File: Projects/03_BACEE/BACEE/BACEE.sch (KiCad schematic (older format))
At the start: 13 parts, among them U1 DS1337_MLv1, U2 24LC1025, U3 24LC1025, U4 ATmega328P-AU, Y1 Crystal, Y2 Crystal

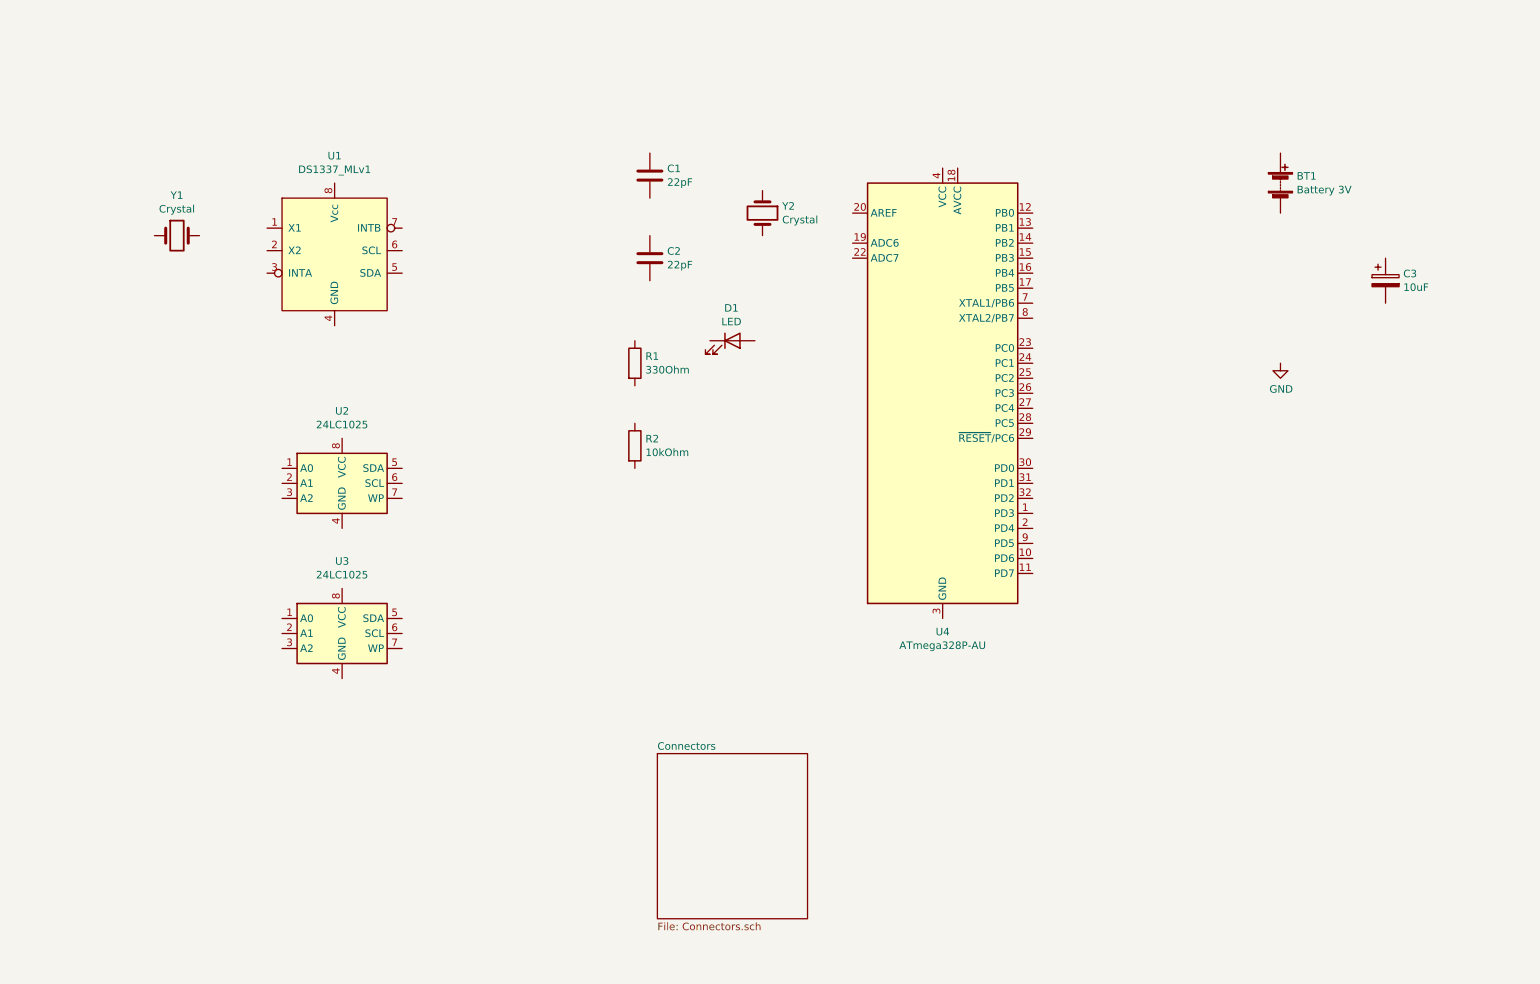
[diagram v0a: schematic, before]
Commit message: Project 3: Complete wiring of connectors hierarchical sheet
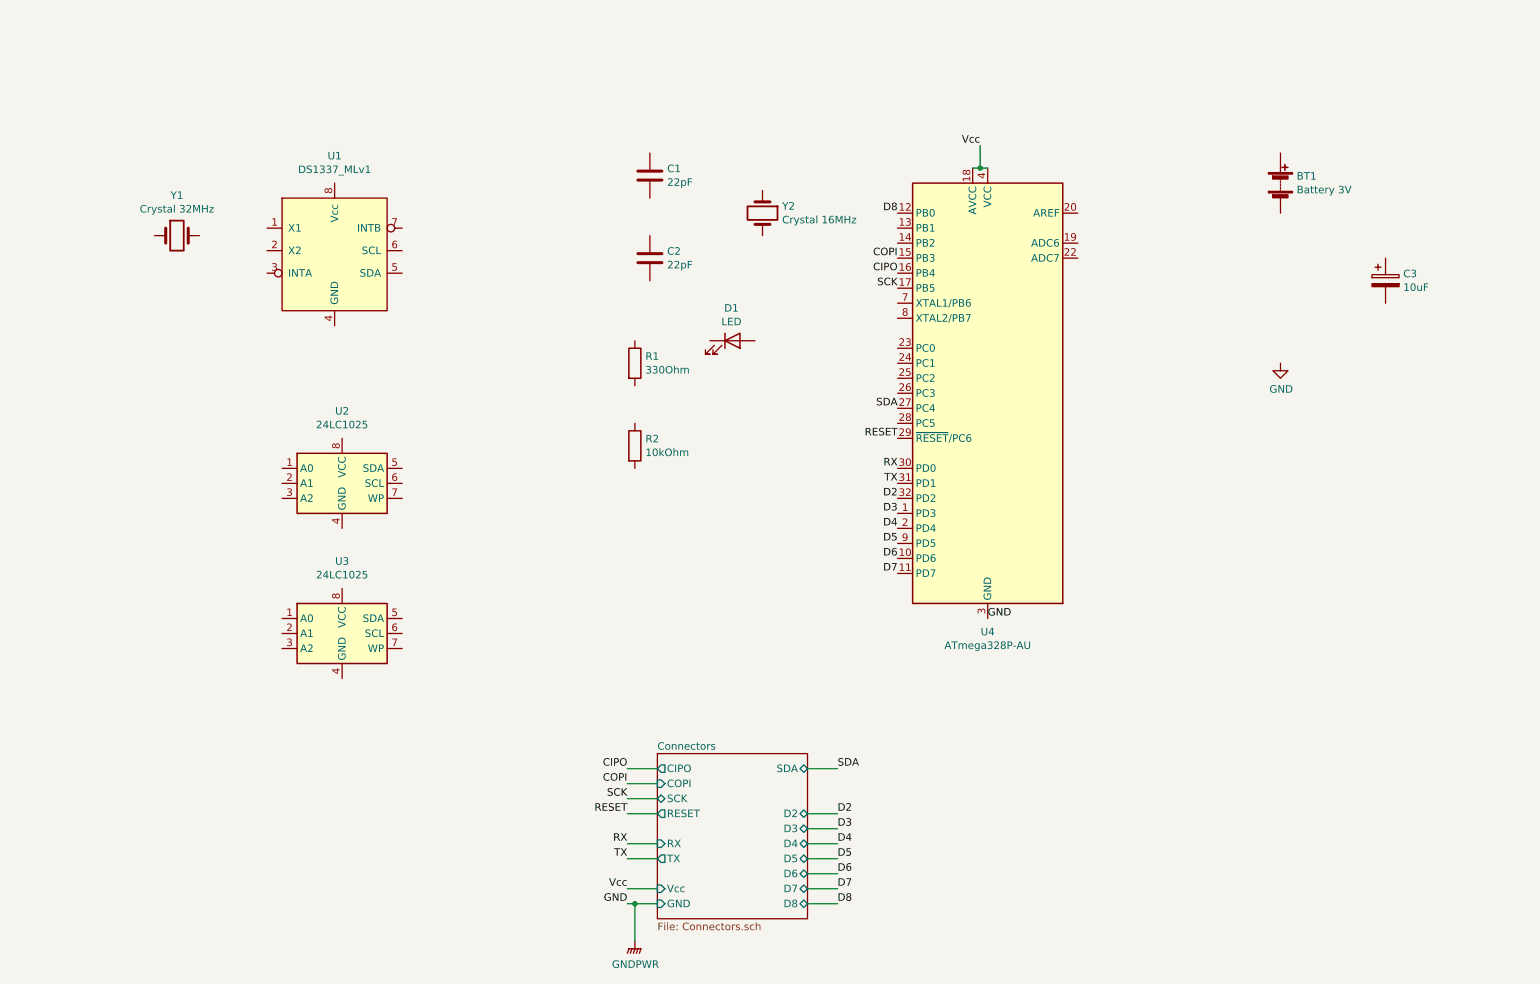
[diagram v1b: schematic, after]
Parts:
- Y1: value Crystal -> Crystal 32MHz
- Y2: value Crystal -> Crystal 16MHz
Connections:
- net GND: now also U4.21 (GND), U4.3 (GND), U4.5 (GND)
- net D3: now reaches U4.1 (PD3)
- net D6: now reaches U4.10 (PD6)
- net D7: now reaches U4.11 (PD7)
- net D8: now reaches U4.12 (PB0)
- net COPI: now reaches U4.15 (PB3)
- net CIPO: now reaches U4.16 (PB4)
- net SCK: now reaches U4.17 (PB5)
- net Vcc: now reaches U4.18 (AVCC)
- net Vcc: now also U4.4 (VCC), U4.6 (VCC)
- net D4: now reaches U4.2 (PD4)
- net SDA: now reaches U4.27 (PC4)
- net RESET: now reaches U4.29 (~RESET~/PC6)
- net RX: now reaches U4.30 (PD0)
- net TX: now reaches U4.31 (PD1)
- net D2: now reaches U4.32 (PD2)
- net D5: now reaches U4.9 (PD5)
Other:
- moved on the sheet: U4
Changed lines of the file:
@@
-	1    0    0    -1
-$EndComp
-$Sheet
-S 5100 5900 1000 1100
-U 61D27AD2
-F0 "Connectors" 50
-F1 "Connectors.sch" 50
-$EndSheet
-$Comp
-L MCU_Microchip_ATmega:ATmega328P-AU U4
-U 1 1 61D2E20A
-P 7000 3500
-F 0 "U4" H 7000 1911 50  0000 C CNN
-F 1 "ATmega328P-AU" H 7000 1820 50  0000 C CNN
-F 2 "Package_QFP:TQFP-32_7x7mm_P0.8mm" H 7000 3500 50  0001 C CIN
-F 3 "http://ww1.microchip.com/downloads/en/DeviceDoc/ATmega328_P%20AVR%20MCU%20with%20picoPower%20Technology%20Data%20Sheet%2040001984A.pdf" H 7000 3500 50  0001 C CNN
-	1    7000 3500
 	1    0    0    -1
 $EndComp
@@
 P 5800 2300
 F 0 "Y2" V 5754 2431 50  0000 L CNN
-F 1 "Crystal" V 5845 2431 50  0000 L CNN
+F 1 "Crystal 16MHz" V 5845 2431 50  0000 L CNN
 F 2 "Crystal:Crystal_SMD_5032-2Pin_5.0x3.2mm_HandSoldering" H 5800 2300 50  0001 C CNN
 F 3 "~" H 5800 2300 50  0001 C CNN
@@
 P 1900 2450
 F 0 "Y1" H 1900 2718 50  0000 C CNN
-F 1 "Crystal" H 1900 2627 50  0000 C CNN
+F 1 "Crystal 32MHz" H 1900 2627 50  0000 C CNN
 F 2 "Crystal:Crystal_SMD_MicroCrystal_CC7V-T1A-2Pin_3.2x1.5mm" H 1900 2450 50  0001 C CNN
 F 3 "~" H 1900 2450 50  0001 C CNN
@@
 	1    0    0    -1
 $EndComp
+Text Label 4900 6000 2    50   ~ 0
+CIPO
+Text Label 6700 2700 2    50   ~ 0
+CIPO
+$Comp
+L MCU_Microchip_ATmega:ATmega328P-AU U4
+U 1 1 61D2E20A
+P 7300 3500
+F 0 "U4" H 7300 1911 50  0000 C CNN
+F 1 "ATmega328P-AU" H 7300 1820 50  0000 C CNN
+F 2 "Package_QFP:TQFP-32_7x7mm_P0.8mm" H 7300 3500 50  0001 C CIN
+F 3 "http://ww1.microchip.com/downloads/en/DeviceDoc/ATmega328_P%20AVR%20MCU%20with%20picoPower%20Technology%20Data%20Sheet%2040001984A.pdf" H 7300 3500 50  0001 C CNN
+	1    7300 3500
+	-1   0    0    -1
+$EndComp
+Wire Wire Line
+	5100 6000 4900 6000
+Text Label 4900 6200 2    50   ~ 0
+SCK
+Wire Wire Line
+	5100 6200 4900 6200
+Text Label 4900 6300 2    50   ~ 0
+RESET
+Wire Wire Line
+	5100 6300 4900 6300
+Text Label 4900 6800 2    50   ~ 0
+Vcc
+Wire Wire Line
+	5100 6800 4900 6800
+Text Label 4900 6100 2    50   ~ 0
+COPI
+Wire Wire Line
+	5100 6100 4900 6100
+Text Label 4900 6900 2    50   ~ 0
+GND
+Wire Wire Line
+	5100 6900 4950 6900
+Text Label 6700 3800 2    50   ~ 0
+RESET
+Text Label 6700 2600 2    50   ~ 0
+COPI
+Text Label 6700 2800 2    50   ~ 0
+SCK
+Text Label 7250 1850 2    50   ~ 0
+Vcc
+Wire Wire Line
+	7200 2000 7250 2000
+Wire Wire Line
+	7250 1850 7250 2000
+Connection ~ 7250 2000
+Wire Wire Line
+	7250 2000 7300 2000
+Text Label 7300 5000 0    50   ~ 0
+GND
+$Comp
+L power:GNDPWR #PWR?
+U 1 1 61D4A407
+P 4950 7150
+F 0 "#PWR?" H 4950 6950 50  0001 C CNN
+F 1 "GNDPWR" H 4954 6996 50  0000 C CNN
+F 2 "" H 4950 7100 50  0001 C CNN
+F 3 "" H 4950 7100 50  0001 C CNN
+	1    4950 7150
+	1    0    0    -1
+$EndComp
+Wire Wire Line
+	4950 7150 4950 6900
+Connection ~ 4950 6900
+Wire Wire Line
+	4950 6900 4900 6900
+Wire Wire Line
+	6300 6000 6100 6000
+Text Label 6300 6000 0    50   ~ 0
+SDA
+Text Label 6700 4300 2    50   ~ 0
+D3
+Text Label 6700 4200 2    50   ~ 0
+D2
+Text Label 6700 4400 2    50   ~ 0
+D4
+Text Label 6700 4500 2    50   ~ 0
+D5
+Text Label 6700 4600 2    50   ~ 0
+D6
+Text Label 6700 4700 2    50   ~ 0
+D7
+Text Label 6700 2300 2    50   ~ 0
+D8
+Text Label 6700 3600 2    50   ~ 0
+SDA
+Wire Wire Line
+	5100 6500 4900 6500
+Wire Wire Line
+	5100 6600 4900 6600
+Text Label 4900 6500 2    50   ~ 0
+RX
+Text Label 4900 6600 2    50   ~ 0
+TX
+Text Label 6700 4000 2    50   ~ 0
+RX
+Text Label 6700 4100 2    50   ~ 0
+TX
+Text Label 6300 6900 0    50   ~ 0
+D8
+Text Label 6300 6800 0    50   ~ 0
+D7
+Text Label 6300 6700 0    50   ~ 0
+D6
+Text Label 6300 6600 0    50   ~ 0
+D5
+Text Label 6300 6500 0    50   ~ 0
+D4
+Text Label 6300 6400 0    50   ~ 0
+D3
+Text Label 6300 6300 0    50   ~ 0
+D2
+Wire Wire Line
+	6300 6900 6100 6900
+Wire Wire Line
+	6300 6800 6100 6800
+Wire Wire Line
+	6300 6700 6100 6700
+Wire Wire Line
+	6300 6600 6100 6600
+Wire Wire Line
+	6300 6500 6100 6500
+Wire Wire Line
+	6300 6400 6100 6400
+Wire Wire Line
+	6300 6300 6100 6300
+$Sheet
+S 5100 5900 1000 1100
+U 61D27AD2
+F0 "Connectors" 50
+F1 "Connectors.sch" 50
+F2 "CIPO" O L 5100 6000 50
+F3 "SCK" B L 5100 6200 50
+F4 "RESET" O L 5100 6300 50
+F5 "Vcc" I L 5100 6800 50
+F6 "COPI" I L 5100 6100 50
+F7 "GND" I L 5100 6900 50
+F8 "RX" I L 5100 6500 50
+F9 "TX" O L 5100 6600 50
+F10 "SDA" B R 6100 6000 50
+F11 "D2" B R 6100 6300 50
+F12 "D3" B R 6100 6400 50
+F13 "D4" B R 6100 6500 50
+F14 "D5" B R 6100 6600 50
+F15 "D6" B R 6100 6700 50
+F16 "D7" B R 6100 6800 50
+F17 "D8" B R 6100 6900 50
+$EndSheet
 $EndSCHEMATC

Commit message: Project 3: Finish wiring and naming nets in root sheet
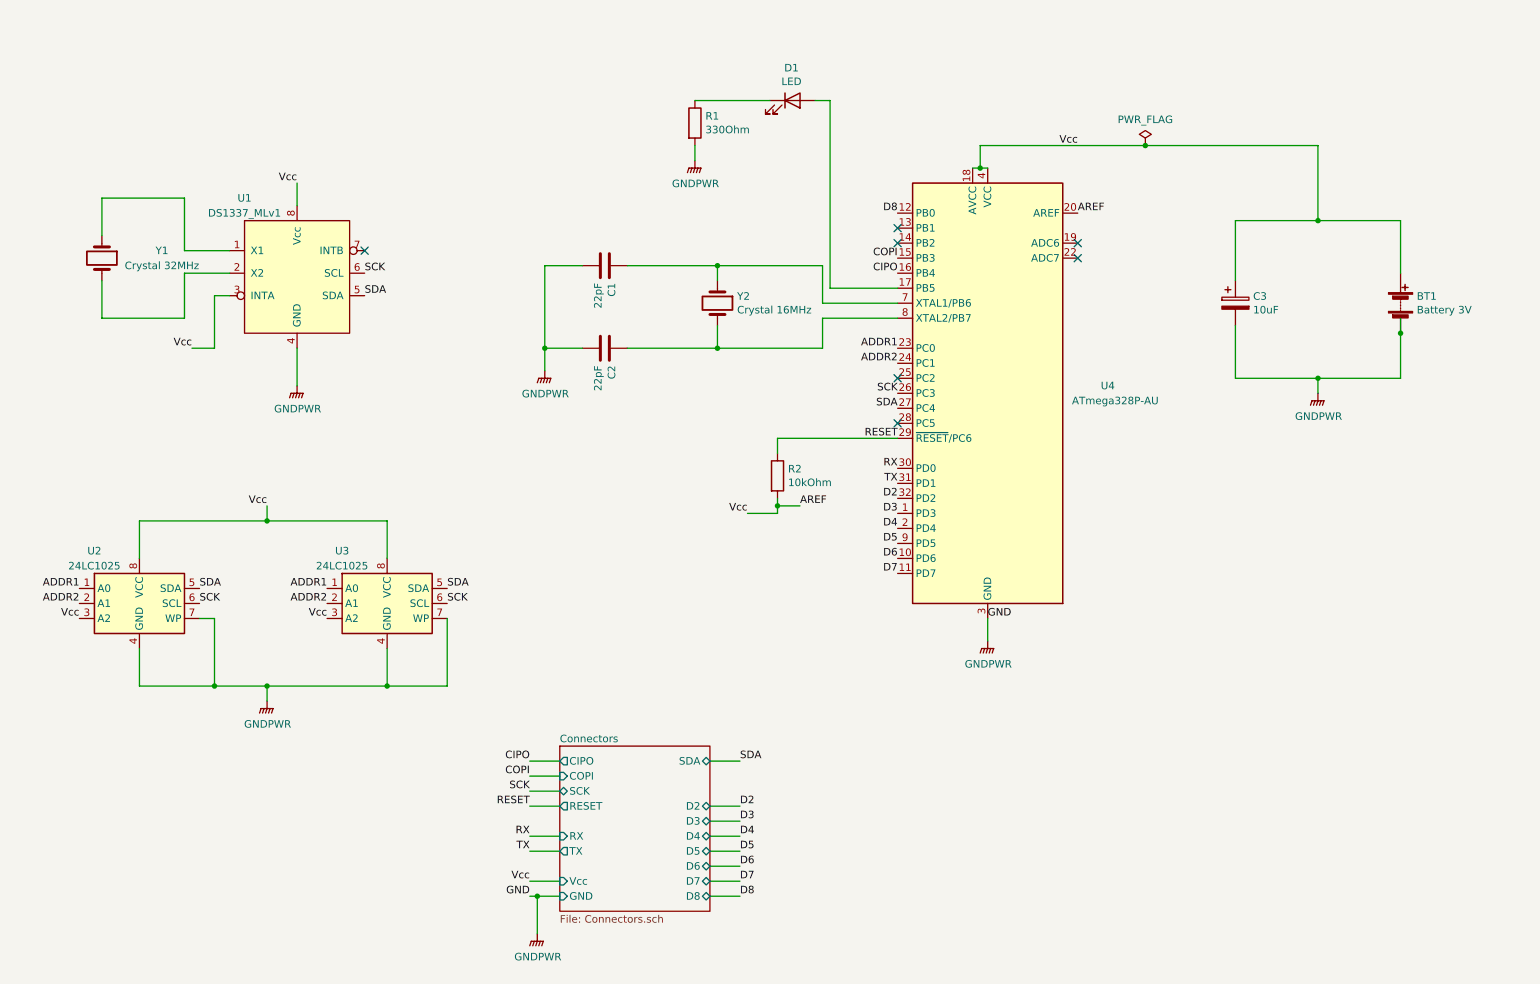
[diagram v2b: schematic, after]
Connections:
- net GND is gone; now on net GNDPWR: U4.21 (GND), U4.3 (GND), U4.5 (GND)
- net Vcc is gone; now on net AREF: U4.18 (AVCC), U4.4 (VCC), U4.6 (VCC)
- net RESET: now also R2.1
- net SCK: now also U1.6 (SCL), U2.6 (SCL), U3.6 (SCL), U4.26 (PC3); no longer U4.17 (PB5)
- net SDA: now also U1.5 (SDA), U2.5 (SDA), U3.5 (SDA)
- net AREF: now reaches BT1.1 (+)
- net AREF: now also C3.1, R2.2, U1.3 (INTA), U1.8 (Vcc), U2.3 (A2), U2.8 (VCC), U3.3 (A2), U3.8 (VCC), U4.20 (AREF)
- net GNDPWR: now reaches BT1.2 (-)
- net GNDPWR: now also C1.2, C2.2, C3.2, R1.2, U1.4 (GND), U2.4 (GND), U2.7 (WP), U3.4 (GND), U3.7 (WP)
- net at D1.1 (K): now also R1.1
- net at D1.2 (A): now also U4.17 (PB5)
- net at C1.1: now also U4.7 (XTAL1/PB6), Y2.1
- net at C2.1: now also U4.8 (XTAL2/PB7), Y2.2
- net ADDR1: now reaches U3.1 (A0)
- net ADDR1: now also U2.1 (A0), U4.23 (PC0)
- net ADDR2: now reaches U3.2 (A1)
- net ADDR2: now also U2.2 (A1), U4.24 (PC1)
- net at U1.1 (X1): now also Y1.1
- net at U1.2 (X2): now also Y1.2
- no-connect marks 0 -> 7
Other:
- moved on the sheet: BT1, C1, C2, C3, D1, R1, R2, U1, U2, U3, Y1, Y2

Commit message: Project 3: Add functional block descriptions and generate netlist
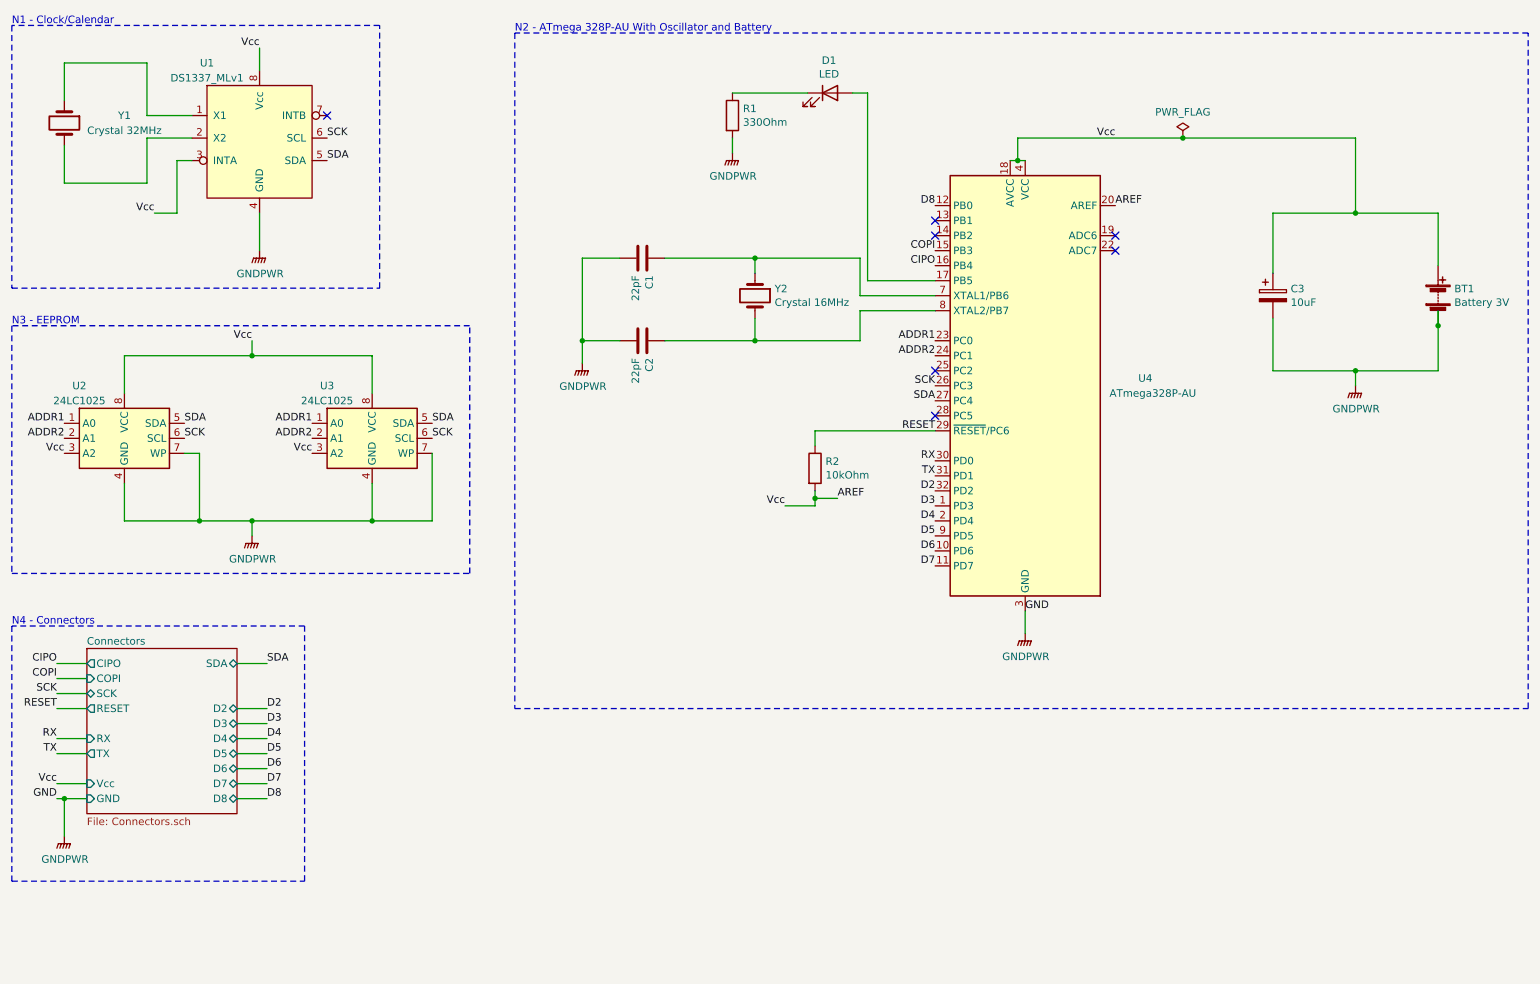
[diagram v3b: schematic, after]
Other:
- note added: "N1 - Clock/Calendar"
- note added: "N2 - ATmega 328P-AU With Oscillator and Battery"
- note added: "N3 - EEPROM"
- note added: "N4 - Connectors"
- moved on the sheet: BT1, C1, C2, C3, D1, R1, R2, U1, U2, U3, U4, Y1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
